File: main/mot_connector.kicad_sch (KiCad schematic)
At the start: 1 part, among them J1501 Conn_02x08_Odd_Even

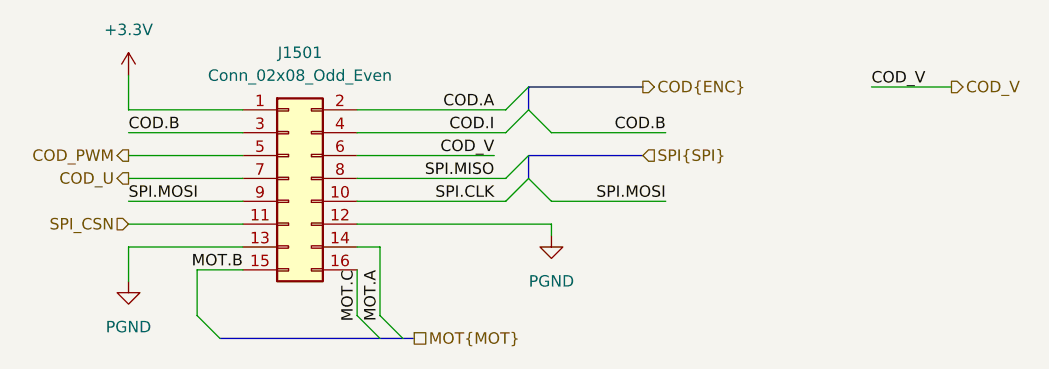
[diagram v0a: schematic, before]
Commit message: Clean silkscreen
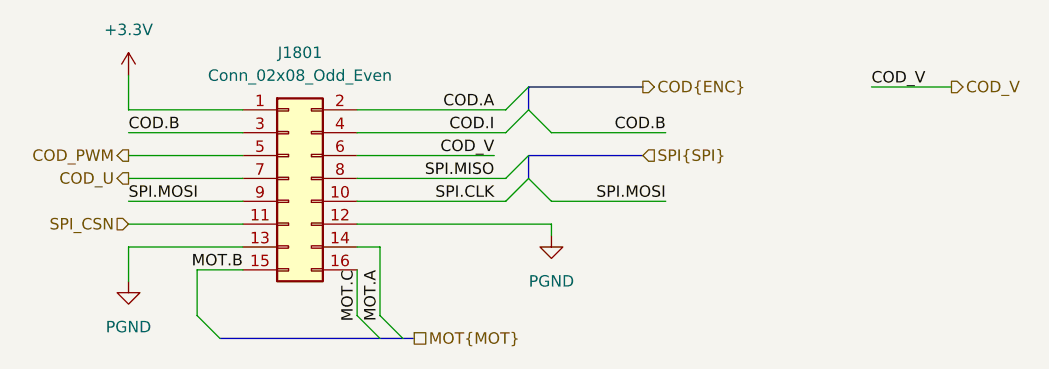
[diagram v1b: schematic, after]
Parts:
- renumbered J1501 to J1801
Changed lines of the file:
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@@
 		(dnp no)
 		(fields_autoplaced yes)
-		(property "Reference" "J1501"
+		(property "Reference" "J1801"
 			(at 147.32 62.23 0)
 			(effects
@@
 			(project "dsv4"
 				(path "/c07e9297-fde8-4755-803e-d05072cd6096/2018e44d-c316-4d67-b4a6-3738e265a76c"
-					(reference "J1501")
+					(reference "J1801")
 					(unit 1)
 				)
@@
 		(dnp no)
 		(fields_autoplaced yes)
-		(property "Reference" "#PWR01502"
+		(property "Reference" "#PWR01802"
 			(at 175.26 88.9 0)
 			(effects
@@
 			(project "dsv4"
 				(path "/c07e9297-fde8-4755-803e-d05072cd6096/2018e44d-c316-4d67-b4a6-3738e265a76c"
-					(reference "#PWR01502")
+					(reference "#PWR01802")
 					(unit 1)
 				)
@@
 		(dnp no)
 		(fields_autoplaced yes)
-		(property "Reference" "#PWR01501"
+		(property "Reference" "#PWR01801"
 			(at 128.27 68.58 0)
 			(effects
@@
 			(project "dsv4"
 				(path "/c07e9297-fde8-4755-803e-d05072cd6096/2018e44d-c316-4d67-b4a6-3738e265a76c"
-					(reference "#PWR01501")
+					(reference "#PWR01801")
 					(unit 1)
 				)
@@
 		(dnp no)
 		(fields_autoplaced yes)
-		(property "Reference" "#PWR01503"
+		(property "Reference" "#PWR01803"
 			(at 128.27 93.98 0)
 			(effects
@@
 			(project "dsv4"
 				(path "/c07e9297-fde8-4755-803e-d05072cd6096/2018e44d-c316-4d67-b4a6-3738e265a76c"
-					(reference "#PWR01503")
-					(unit 1)
-				)
+					(reference "#PWR01803")
+					(unit 1)
+				)

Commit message: Revised with BOM ordered
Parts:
- J1801: MPN (none) -> 22-28-4162; Mouser SKU (none) -> 538-22-28-4162
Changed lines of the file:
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@@
+			)
+		)
+		(property "MPN" "22-28-4162 "
+			(at 146.05 76.2 0)
+			(effects
+				(font
+					(size 1.27 1.27)
+				)
+			)
+		)
+		(property "Mouser SKU" " 538-22-28-4162 "
+			(at 146.05 76.2 0)
+			(effects
+				(font
+					(size 1.27 1.27)
+				)
 			)
 		)
